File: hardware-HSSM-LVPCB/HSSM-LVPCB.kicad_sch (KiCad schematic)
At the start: 67 parts, among them J1 UFL_R_SMT_1_10, Q1 Q_MOSFET_N_BSS123, Q2 Q_MOSFET_N_BSS123, U1 ESP32-C6, U2 W25Q64JVSSIQ_SOIC-8, U3 U_USB_UART_CP2102-GMR, U4 U_EnvSensor_BME280_LGA_Bosch, U5 U_AirQualitySensor_ENS160_BGLM, X1 X_40MHz_SMD_ECS-2520SMV-400-F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

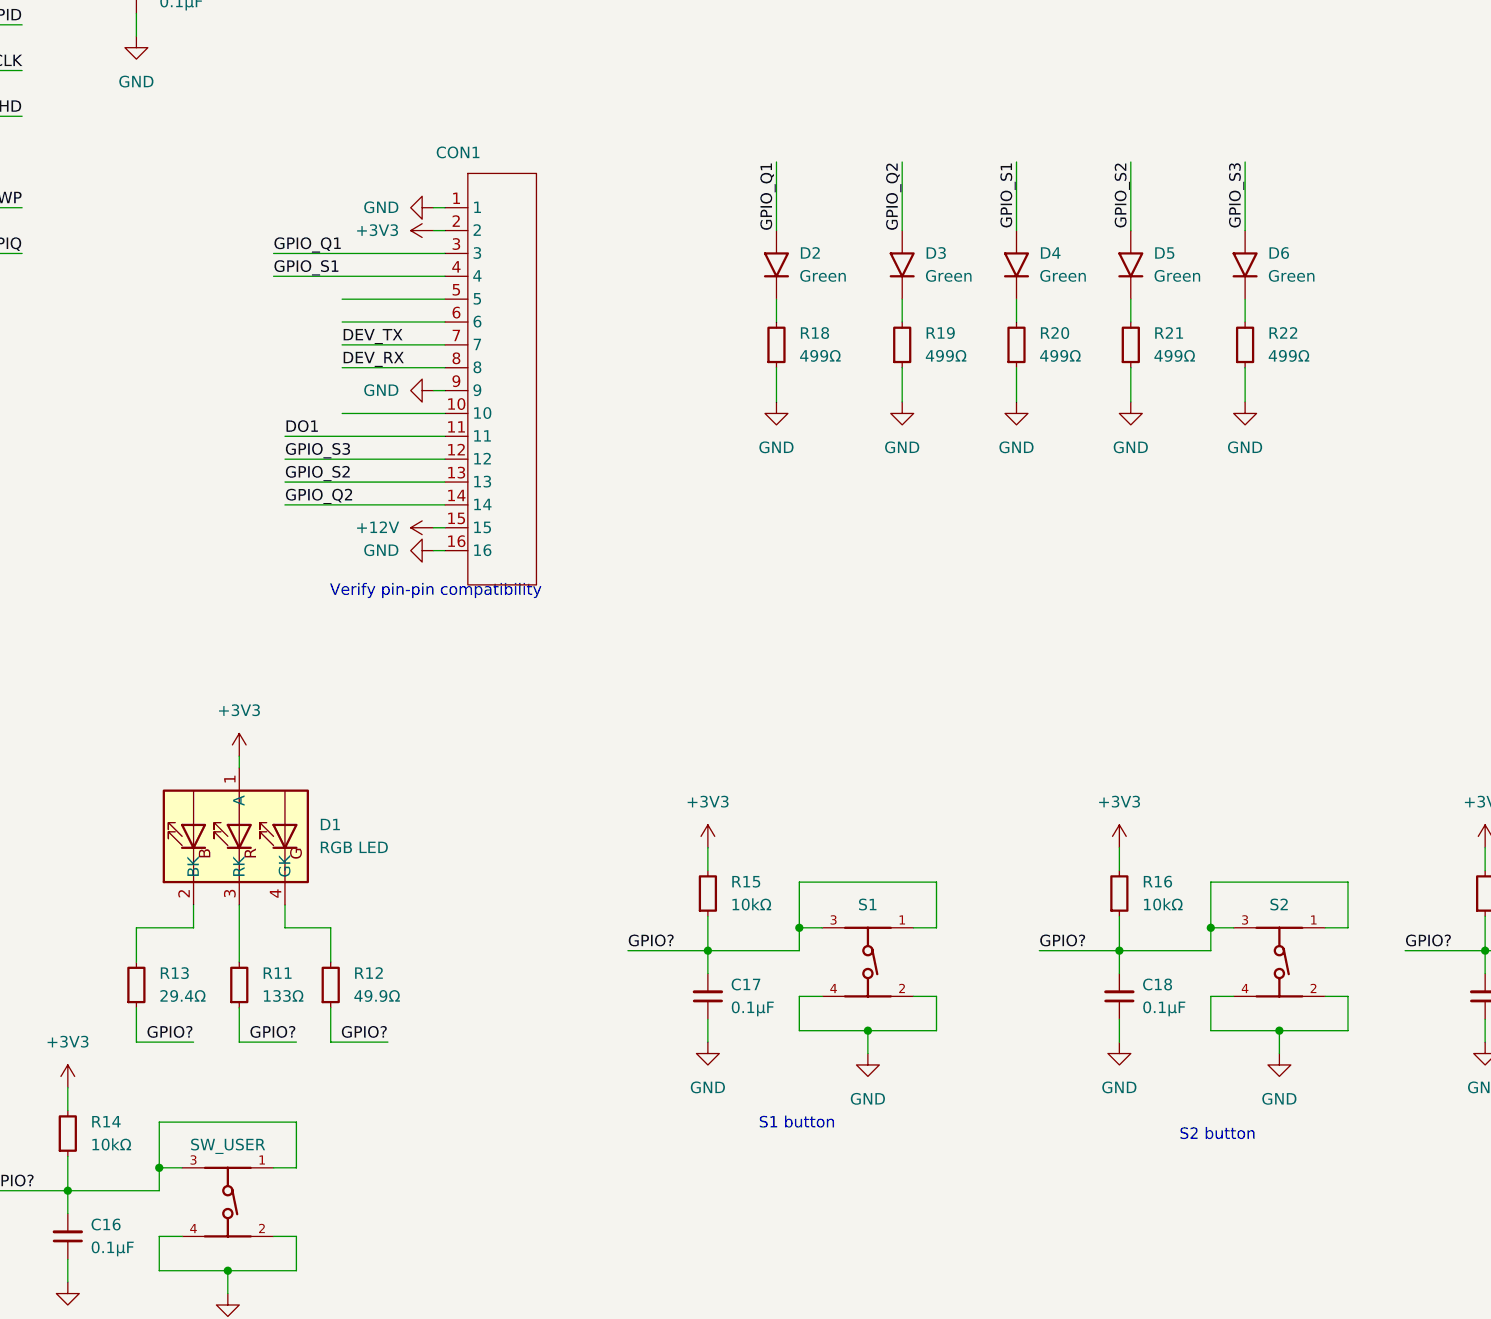
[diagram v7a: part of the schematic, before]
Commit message: [#9] Replace LEDs
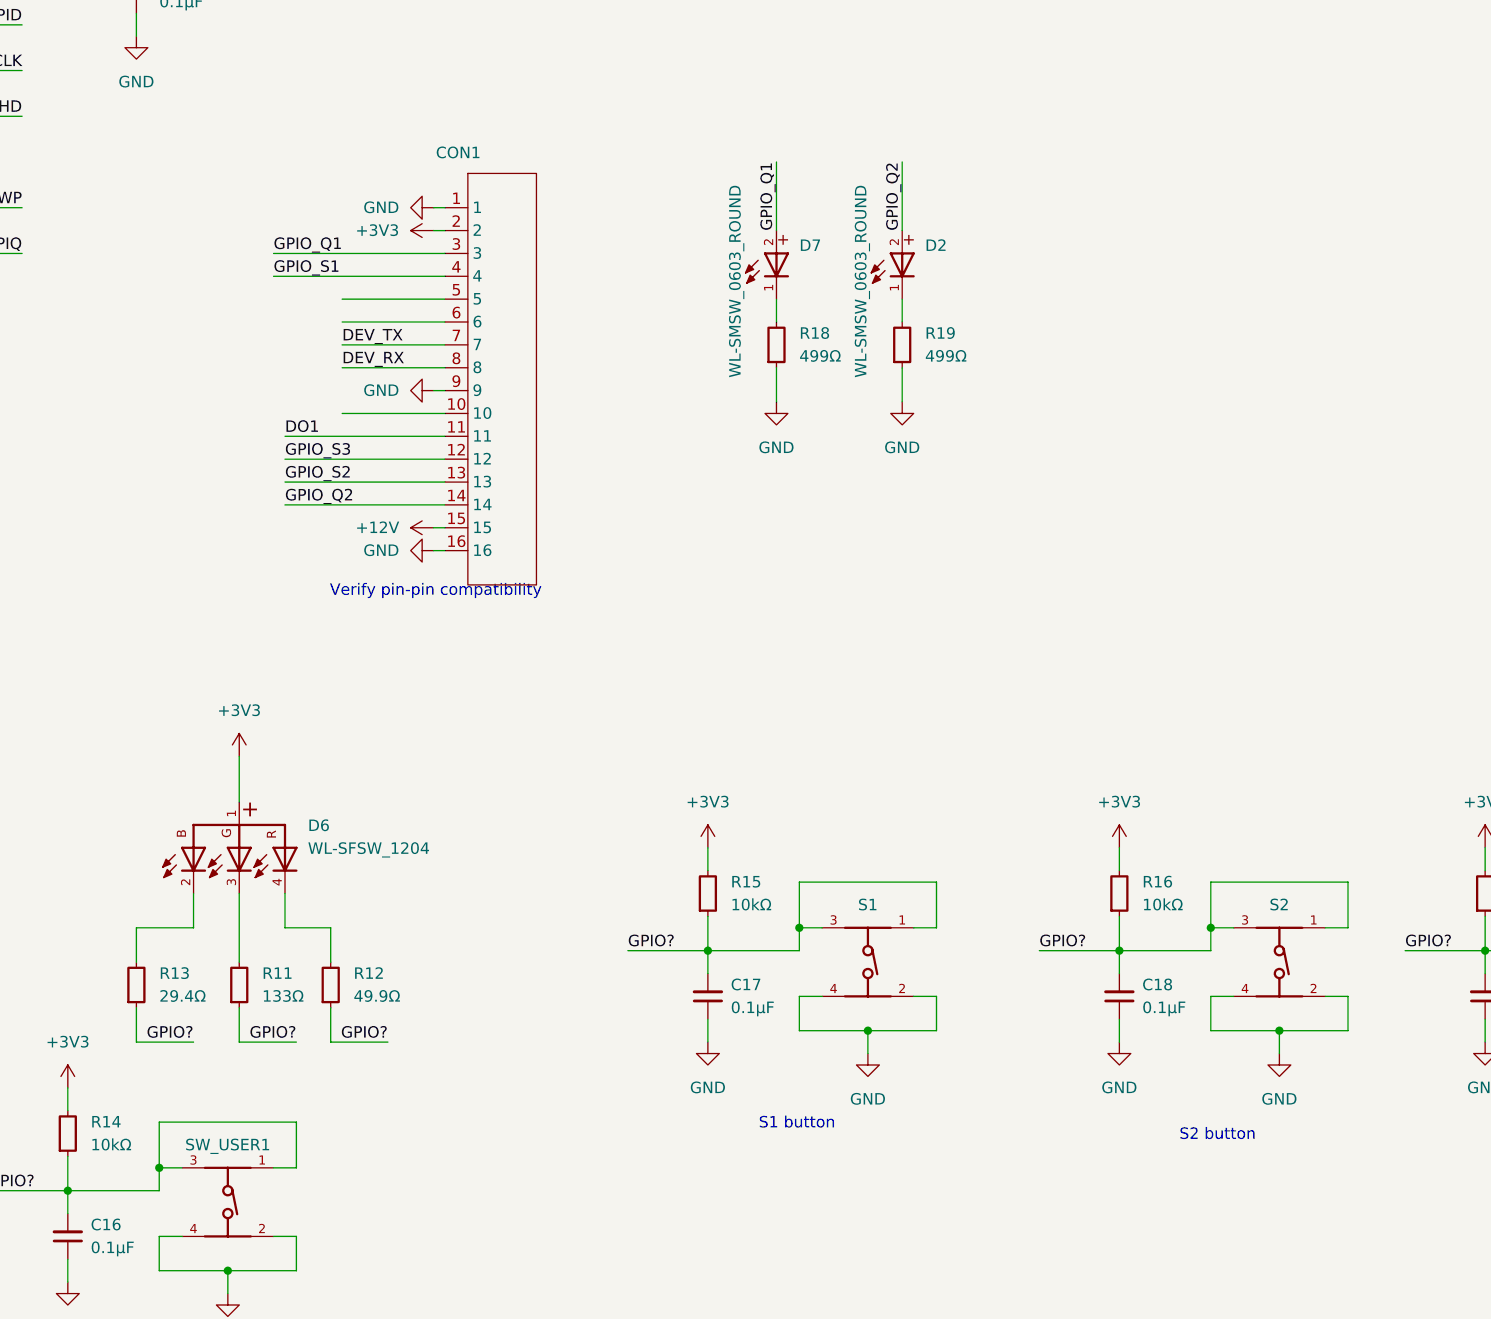
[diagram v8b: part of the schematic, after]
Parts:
- removed D1: LED_RGB_WL-SFTW_155124M173200, HSSM-LVPCB:LED_1515, symbol HSSM-LVPCB:LED_RGB_WL-SFTW_155124M173200
- removed D2, D3, D4, D5, D6: LED_Green_1.6x0.8mm_SMD_KPTD-1608ZGC, HSSM-LVPCB:LED_0603_1608Metric, symbol HSSM-LVPCB:LED_Green_1.6x0.8mm_SMD_KPTD-1608ZGC
- removed R20, R21, R22: R_499R_1pct_0402_RC0402FR-07499RL, HSSM-LVPCB:R_0402, symbol HSSM-LVPCB:R_499R_1pct_0402_RC0402FR-07499RL
- added D2, D7: WL-SMSW_0603_ROUND, HSSM-LVPCB:155060AS73200, symbol HSSM-LVPCB:LED_Amber_angle_155060AS73200
- added D6: WL-SFSW_1204, HSSM-LVPCB:155124M173200, symbol HSSM-LVPCB:LED_RGB_angle_155124M173200
- renumbered SW_USER to SW_USER1
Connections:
- net +3V3: now also D6.1
- net GPIO_Q1: now also D7.2
- net GPIO_Q2: now also D2.2
- net at R13.2: now also D6.2
- net at R11.2: now also D6.3
- net at R19.2: now also D2.1
- net at R12.2: now also D6.4
- net at R18.2: now also D7.1
